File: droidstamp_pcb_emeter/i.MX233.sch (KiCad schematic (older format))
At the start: 90 parts, among them IC1 iMX233, J1 MICROSD, P1 CONN_12X2, P10 CONN_1, P2 CONN_12X2, P3 CONN_1, P4 CONN_4X2, P5 CONN_1, P7 CONN_1, Q1 MMDT3904, U1 ADM3101E, U3 M25P32, X1 24MHz

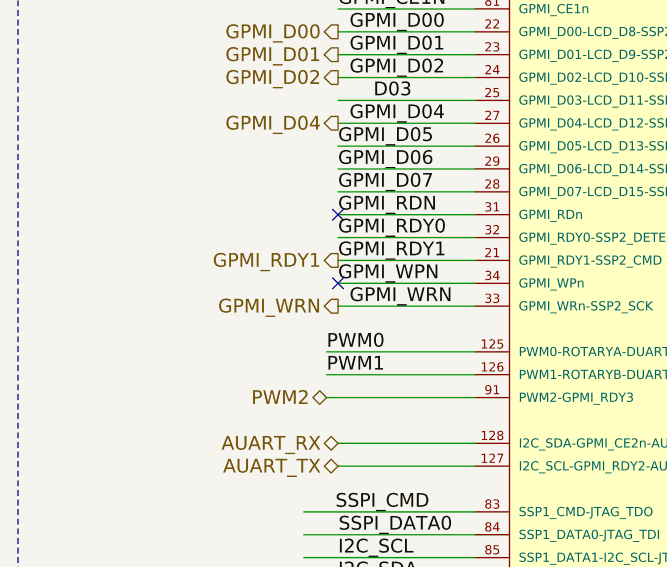
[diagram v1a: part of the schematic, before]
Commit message: Adición de la linea BOOT_MODE para modificar el inicio del stm32 desde memoria interna o jtag
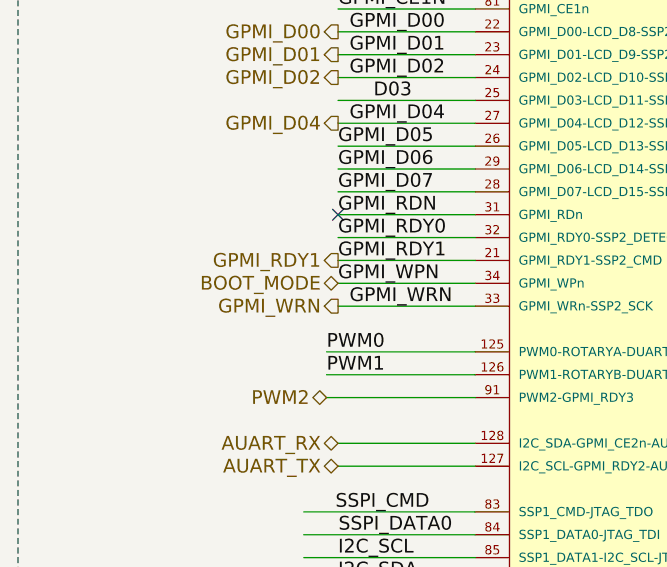
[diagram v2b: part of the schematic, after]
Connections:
- net labels added: BOOT_MODE
- no-connect marks 9 -> 8
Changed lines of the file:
@@
-EESchema Schematic File Version 2  date vie 20 abr 2012 12:34:33 COT
+EESchema Schematic File Version 2  date Tue 21 Aug 2012 09:23:05 AM COT
 LIBS:con-jack
 LIBS:zxct1009
@@
 Sheet 2 5
 Title ""
-Date "20 apr 2012"
+Date "21 aug 2012"
 Rev ""
 Comp ""
@@
 Comment4 ""
 $EndDescr
+Text HLabel 1950 6000 0    60   BiDi ~ 0
+BOOT_MODE
 NoConn ~ 13600 5100
 Wire Notes Line
@@
 	1    0    0    -1
 $EndComp
-NoConn ~ 1950 6000
 NoConn ~ 1950 5700
 Text Notes 9650 6450 0    60   ~ 0
